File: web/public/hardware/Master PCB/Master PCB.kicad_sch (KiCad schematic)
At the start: 41 parts, among them J1 SWD Conn, J10 LED3, J11 LDR4, J12 LED4, J13 LED Conn, J2 OLED1, J3 OLED2, J4 5V_IN, J5 LDR1, J6 LED1, J7 LDR2, J8 LED2, J9 LDR3

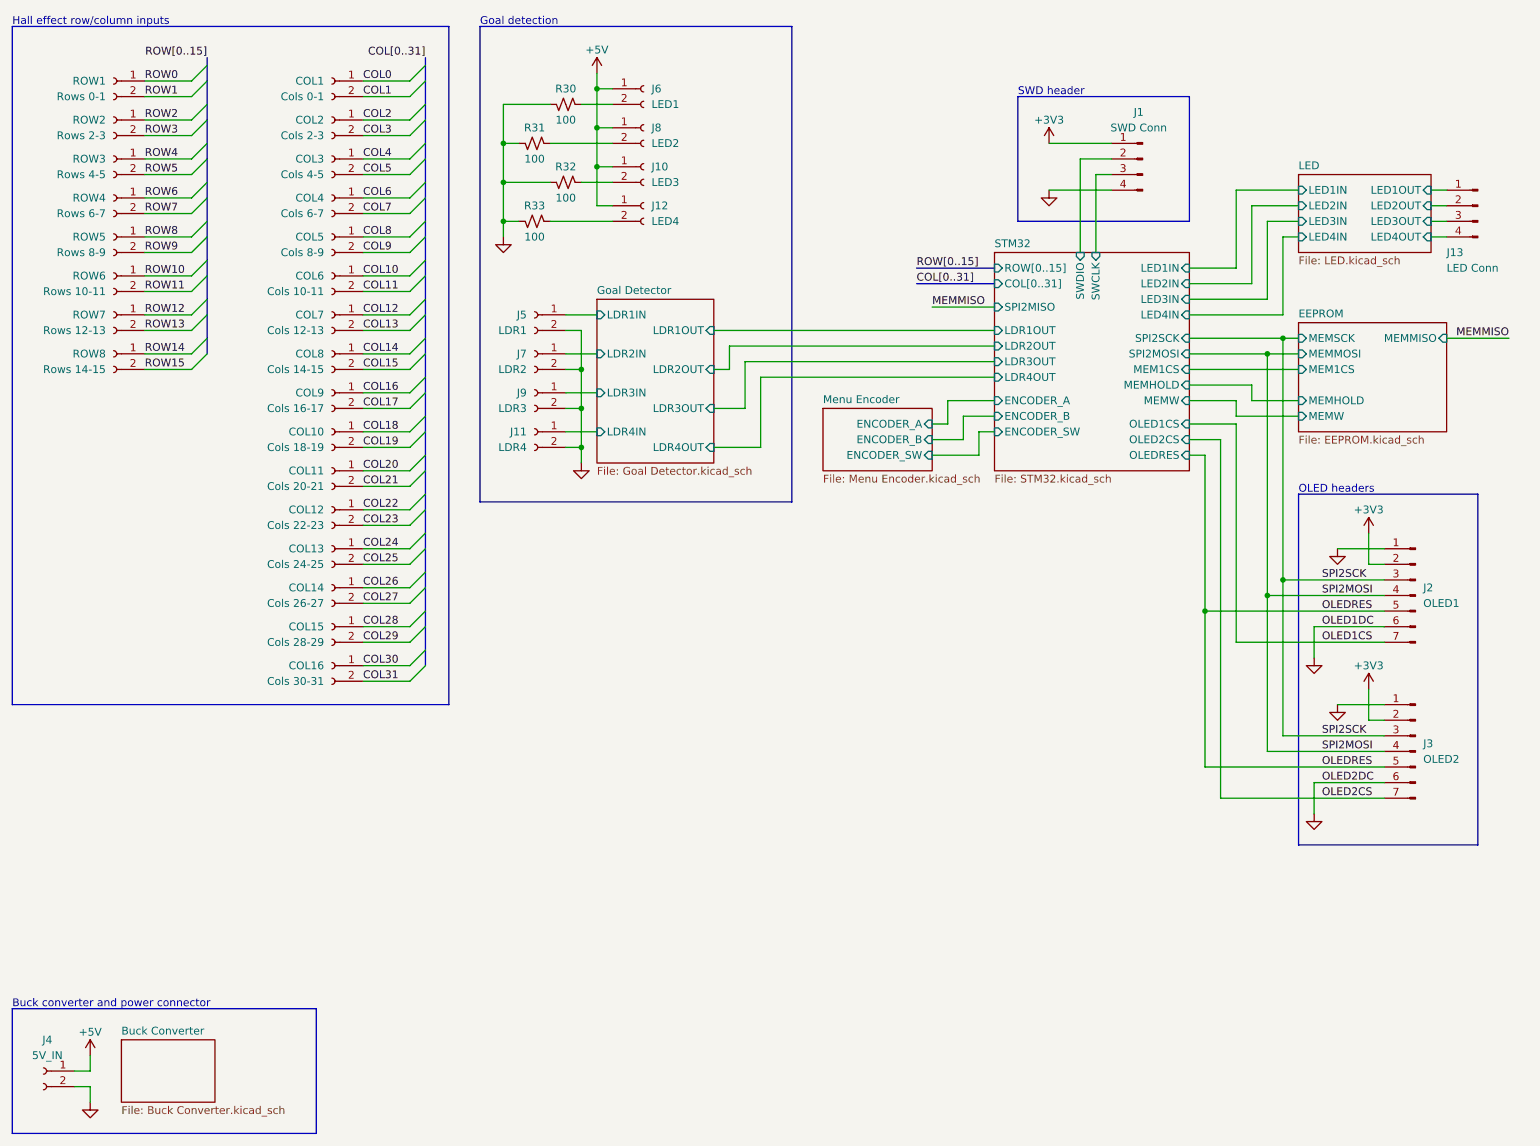
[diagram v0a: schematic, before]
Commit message: Add missing signals to master PCB for relay and OLED DC, add mounting holes, add text, add dimensions
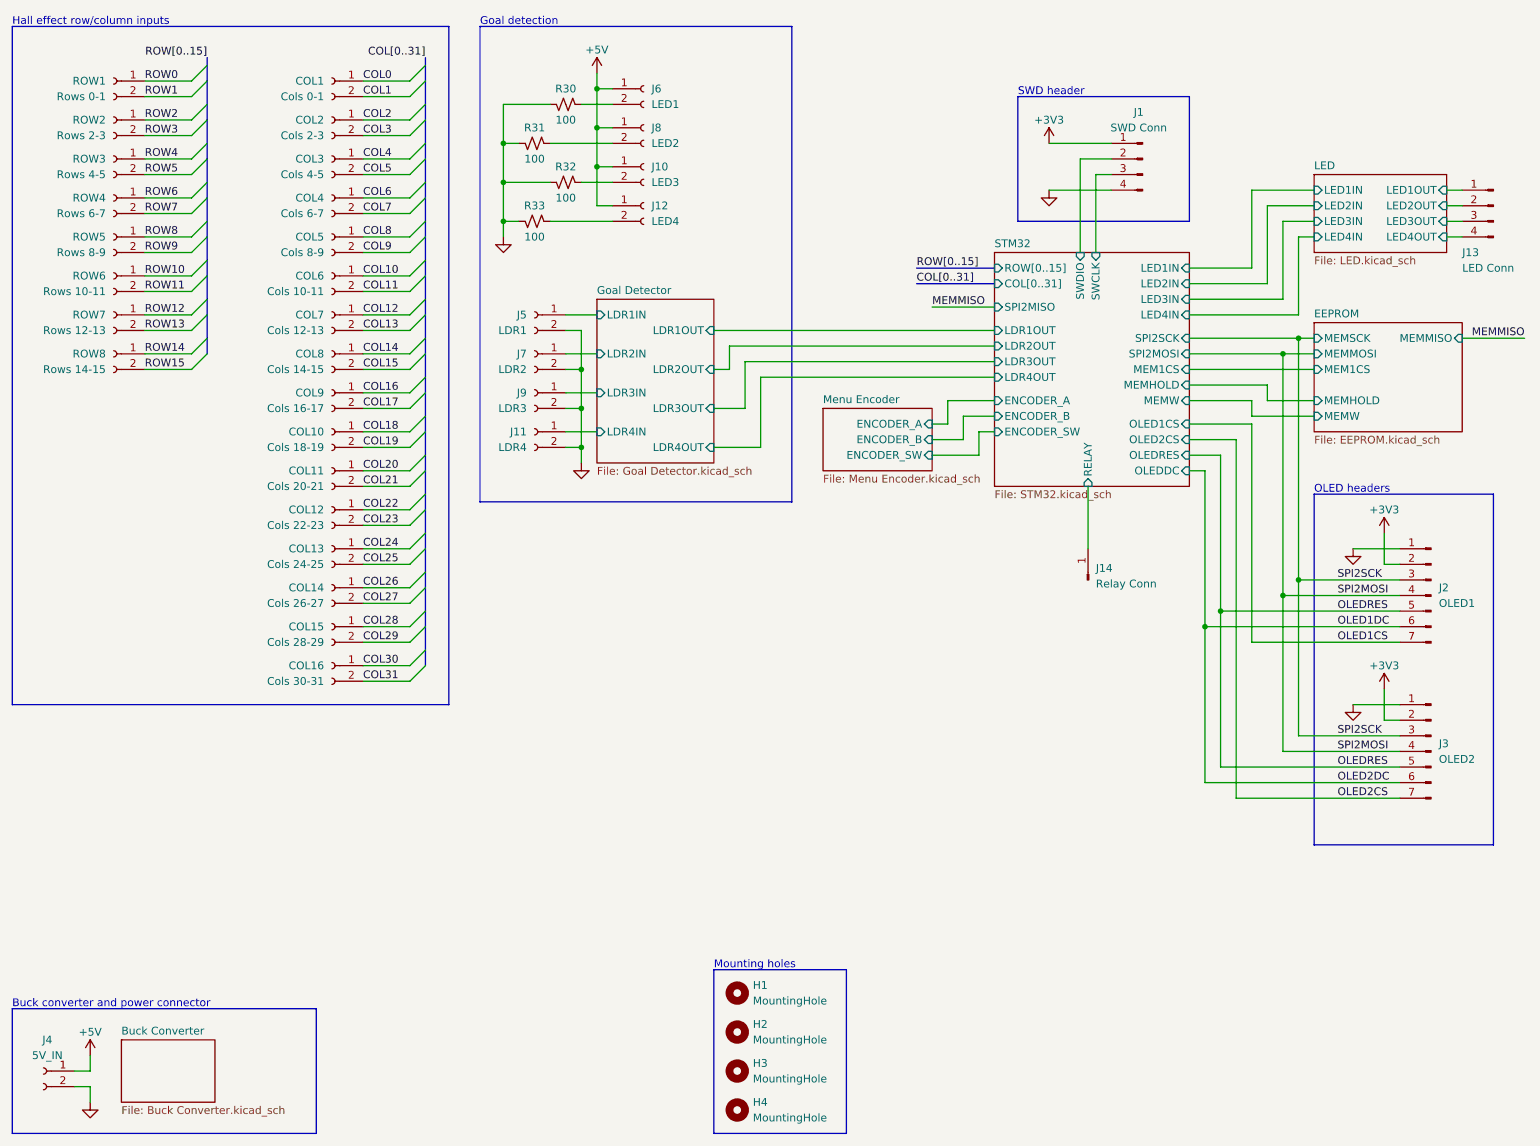
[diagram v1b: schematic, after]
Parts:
- added H1, H2, H3, H4: MountingHole, MountingHole:MountingHole_3.2mm_M3, symbol Mechanical:MountingHole
- added J14: Relay Conn, Connector_PinHeader_2.54mm:PinHeader_1x01_P2.54mm_Vertical, symbol Connector:Conn_01x01_Pin
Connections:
- net GND: no longer J2.6 (Pin_6), J3.6 (Pin_6)
- new net OLED1DC: J2.6 (Pin_6), J3.6 (Pin_6)
- new net STM32/RELAY: J14.1 (Pin_1)
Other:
- sheet STM32 ports: added OLEDDC, RELAY; removed none
- note added: "Mounting holes"
- moved on the sheet: J13, J2, J3

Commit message: Change STM32 pinout, begin placing components on new PCB
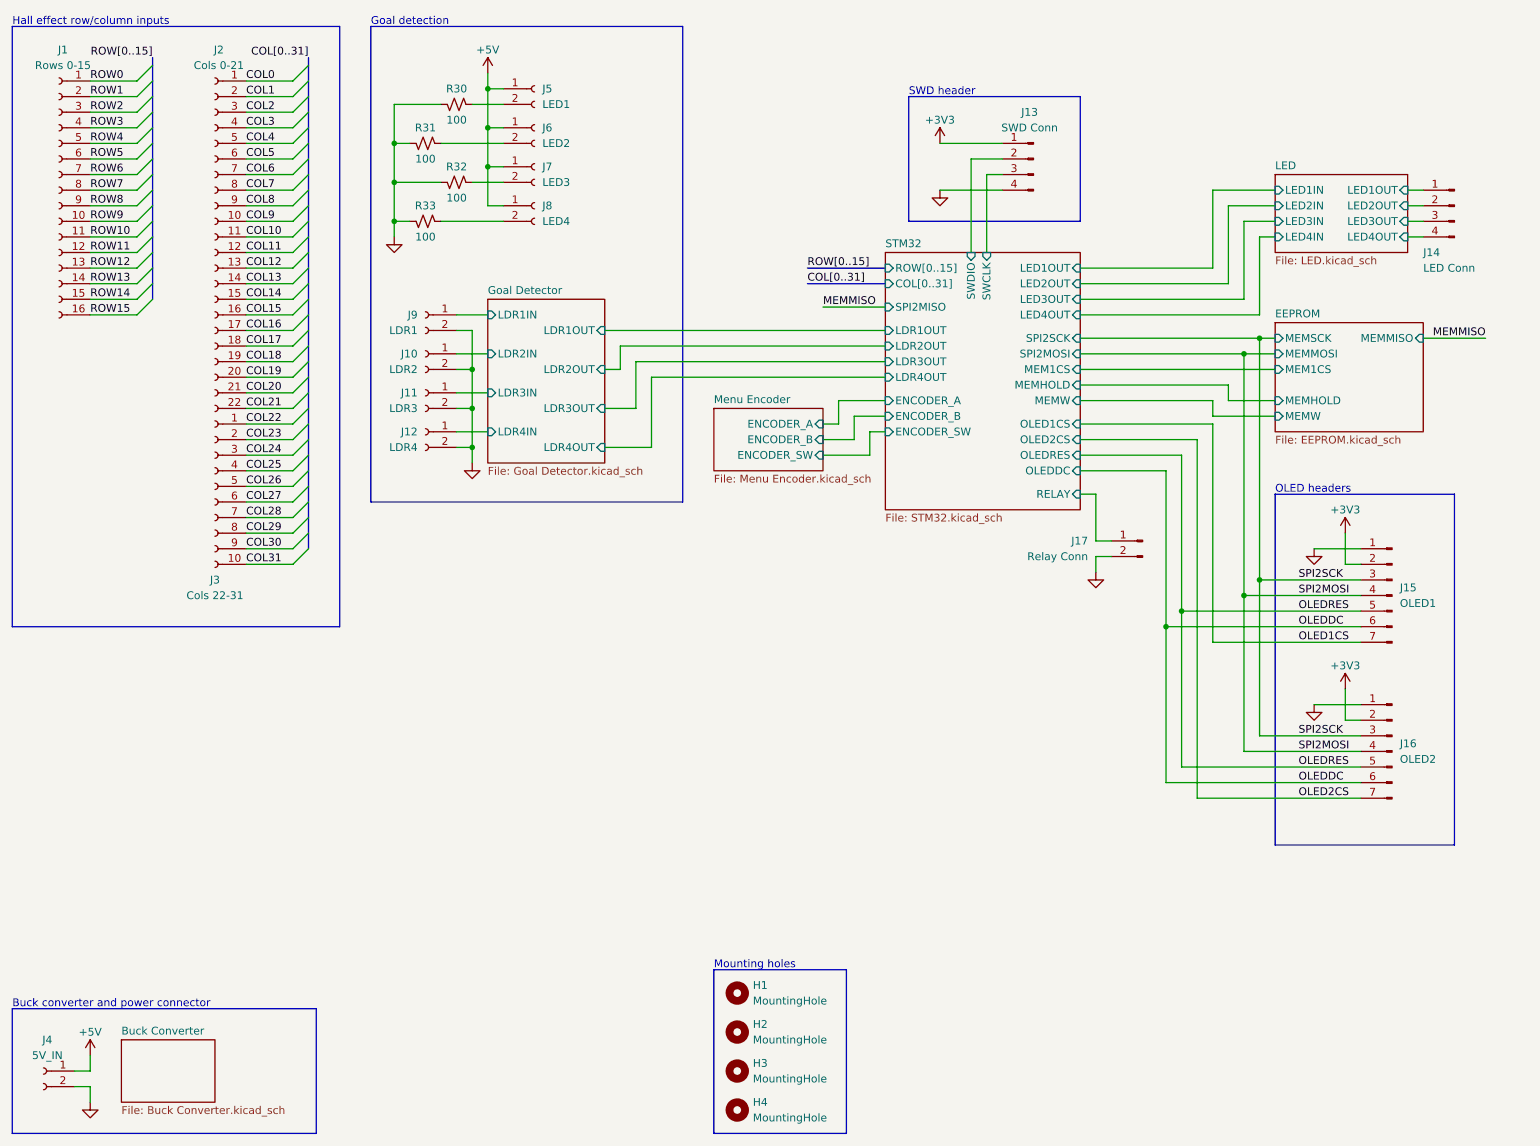
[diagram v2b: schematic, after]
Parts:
- removed COL1: Cols 0-1, Connector_PinHeader_2.54mm:PinHeader_1x02_P2.54mm_Vertical, symbol Connector:Conn_01x02_Socket
- removed COL10: Cols 18-19, Connector_PinHeader_2.54mm:PinHeader_1x02_P2.54mm_Vertical, symbol Connector:Conn_01x02_Socket
- removed COL11: Cols 20-21, Connector_PinHeader_2.54mm:PinHeader_1x02_P2.54mm_Vertical, symbol Connector:Conn_01x02_Socket
- removed COL12: Cols 22-23, Connector_PinHeader_2.54mm:PinHeader_1x02_P2.54mm_Vertical, symbol Connector:Conn_01x02_Socket
- removed COL13: Cols 24-25, Connector_PinHeader_2.54mm:PinHeader_1x02_P2.54mm_Vertical, symbol Connector:Conn_01x02_Socket
- removed COL14: Cols 26-27, Connector_PinHeader_2.54mm:PinHeader_1x02_P2.54mm_Vertical, symbol Connector:Conn_01x02_Socket
- removed COL15: Cols 28-29, Connector_PinHeader_2.54mm:PinHeader_1x02_P2.54mm_Vertical, symbol Connector:Conn_01x02_Socket
- removed COL16: Cols 30-31, Connector_PinHeader_2.54mm:PinHeader_1x02_P2.54mm_Vertical, symbol Connector:Conn_01x02_Socket
- removed COL2: Cols 2-3, Connector_PinHeader_2.54mm:PinHeader_1x02_P2.54mm_Vertical, symbol Connector:Conn_01x02_Socket
- removed COL3: Cols 4-5, Connector_PinHeader_2.54mm:PinHeader_1x02_P2.54mm_Vertical, symbol Connector:Conn_01x02_Socket
- removed COL4: Cols 6-7, Connector_PinHeader_2.54mm:PinHeader_1x02_P2.54mm_Vertical, symbol Connector:Conn_01x02_Socket
- removed COL5: Cols 8-9, Connector_PinHeader_2.54mm:PinHeader_1x02_P2.54mm_Vertical, symbol Connector:Conn_01x02_Socket
- removed COL6: Cols 10-11, Connector_PinHeader_2.54mm:PinHeader_1x02_P2.54mm_Vertical, symbol Connector:Conn_01x02_Socket
- removed COL7: Cols 12-13, Connector_PinHeader_2.54mm:PinHeader_1x02_P2.54mm_Vertical, symbol Connector:Conn_01x02_Socket
- removed COL8: Cols 14-15, Connector_PinHeader_2.54mm:PinHeader_1x02_P2.54mm_Vertical, symbol Connector:Conn_01x02_Socket
- removed COL9: Cols 16-17, Connector_PinHeader_2.54mm:PinHeader_1x02_P2.54mm_Vertical, symbol Connector:Conn_01x02_Socket
- removed J14: Relay Conn, Connector_PinHeader_2.54mm:PinHeader_1x01_P2.54mm_Vertical, symbol Connector:Conn_01x01_Pin
- removed ROW1: Rows 0-1, Connector_PinHeader_2.54mm:PinHeader_1x02_P2.54mm_Vertical, symbol Connector:Conn_01x02_Socket
- removed ROW2: Rows 2-3, Connector_PinHeader_2.54mm:PinHeader_1x02_P2.54mm_Vertical, symbol Connector:Conn_01x02_Socket
- removed ROW3: Rows 4-5, Connector_PinHeader_2.54mm:PinHeader_1x02_P2.54mm_Vertical, symbol Connector:Conn_01x02_Socket
- removed ROW4: Rows 6-7, Connector_PinHeader_2.54mm:PinHeader_1x02_P2.54mm_Vertical, symbol Connector:Conn_01x02_Socket
- removed ROW5: Rows 8-9, Connector_PinHeader_2.54mm:PinHeader_1x02_P2.54mm_Vertical, symbol Connector:Conn_01x02_Socket
- removed ROW6: Rows 10-11, Connector_PinHeader_2.54mm:PinHeader_1x02_P2.54mm_Vertical, symbol Connector:Conn_01x02_Socket
- removed ROW7: Rows 12-13, Connector_PinHeader_2.54mm:PinHeader_1x02_P2.54mm_Vertical, symbol Connector:Conn_01x02_Socket
- removed ROW8: Rows 14-15, Connector_PinHeader_2.54mm:PinHeader_1x02_P2.54mm_Vertical, symbol Connector:Conn_01x02_Socket
- added J1: Rows 0-15, Connector_PinHeader_2.54mm:PinHeader_1x16_P2.54mm_Vertical, symbol Connector:Conn_01x16_Socket
- added J17: Relay Conn, Connector_JST:JST_PH_S2B-PH-SM4-TB_1x02-1MP_P2.00mm_Horizontal, symbol Connector:Conn_01x02_Pin
- added J2: Cols 0-21, Connector_PinHeader_2.54mm:PinHeader_1x22_P2.54mm_Vertical, symbol Connector:Conn_01x22_Socket
- added J3: Cols 22-31, Connector_PinHeader_2.54mm:PinHeader_1x10_P2.54mm_Vertical, symbol Connector:Conn_01x10_Socket
- J10: renamed from J7; footprint Connector_PinHeader_2.54mm:PinHeader_1x02_P2.54mm_Vertical -> Connector_JST:JST_PH_S2B-PH-SM4-TB_1x02-1MP_P2.00mm_Horizontal
- J11: renamed from J9; footprint Connector_PinHeader_2.54mm:PinHeader_1x02_P2.54mm_Vertical -> Connector_JST:JST_PH_S2B-PH-SM4-TB_1x02-1MP_P2.00mm_Horizontal
- J12: renamed from J11; footprint Connector_PinHeader_2.54mm:PinHeader_1x02_P2.54mm_Vertical -> Connector_JST:JST_PH_S2B-PH-SM4-TB_1x02-1MP_P2.00mm_Horizontal
- J15: renamed from J2; footprint Connector_PinHeader_2.54mm:PinHeader_1x07_P2.54mm_Vertical -> Connector_JST:JST_PH_S7B-PH-SM4-TB_1x07-1MP_P2.00mm_Horizontal
- J16: renamed from J3; footprint Connector_PinHeader_2.54mm:PinHeader_1x07_P2.54mm_Vertical -> Connector_JST:JST_PH_S7B-PH-SM4-TB_1x07-1MP_P2.00mm_Horizontal
- J4: footprint Connector_PinHeader_2.54mm:PinHeader_1x02_P2.54mm_Vertical -> Connector_JST:JST_PH_S2B-PH-SM4-TB_1x02-1MP_P2.00mm_Horizontal
- J5: renamed from J6; footprint Connector_PinHeader_2.54mm:PinHeader_1x02_P2.54mm_Vertical -> Connector_JST:JST_PH_S2B-PH-SM4-TB_1x02-1MP_P2.00mm_Horizontal
- J6: renamed from J8; footprint Connector_PinHeader_2.54mm:PinHeader_1x02_P2.54mm_Vertical -> Connector_JST:JST_PH_S2B-PH-SM4-TB_1x02-1MP_P2.00mm_Horizontal
- J7: renamed from J10; footprint Connector_PinHeader_2.54mm:PinHeader_1x02_P2.54mm_Vertical -> Connector_JST:JST_PH_S2B-PH-SM4-TB_1x02-1MP_P2.00mm_Horizontal
- J8: renamed from J12; footprint Connector_PinHeader_2.54mm:PinHeader_1x02_P2.54mm_Vertical -> Connector_JST:JST_PH_S2B-PH-SM4-TB_1x02-1MP_P2.00mm_Horizontal
- J9: renamed from J5; footprint Connector_PinHeader_2.54mm:PinHeader_1x02_P2.54mm_Vertical -> Connector_JST:JST_PH_S2B-PH-SM4-TB_1x02-1MP_P2.00mm_Horizontal
- renumbered J1 to J13, J13 to J14
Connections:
- net COL0: now also J2.1 (Pin_1)
- net COL1: now also J2.2 (Pin_2)
- net COL10: now also J2.11 (Pin_11)
- net COL11: now also J2.12 (Pin_12)
- net COL12: now also J2.13 (Pin_13)
- net COL13: now also J2.14 (Pin_14)
- net COL14: now also J2.15 (Pin_15)
- net COL15: now also J2.16 (Pin_16)
- net COL16: now also J2.17 (Pin_17)
- net COL17: now also J2.18 (Pin_18)
- net COL18: now also J2.19 (Pin_19)
- net COL19: now also J2.20 (Pin_20)
- net COL2: now also J2.3 (Pin_3)
- net COL20: now also J2.21 (Pin_21)
- net COL21: now also J2.22 (Pin_22)
- net COL22: now also J3.1 (Pin_1)
- net COL23: now also J3.2 (Pin_2)
- net COL24: now also J3.3 (Pin_3)
- net COL25: now also J3.4 (Pin_4)
- net COL26: now also J3.5 (Pin_5)
- net COL27: now also J3.6 (Pin_6)
- net COL28: now also J3.7 (Pin_7)
- net COL29: now also J3.8 (Pin_8)
- net COL3: now also J2.4 (Pin_4)
- net COL30: now also J3.9 (Pin_9)
- net COL31: now also J3.10 (Pin_10)
- net COL4: now also J2.5 (Pin_5)
- net COL5: now also J2.6 (Pin_6)
- net COL6: now also J2.7 (Pin_7)
- net COL7: now also J2.8 (Pin_8)
- net COL8: now also J2.9 (Pin_9)
- net COL9: now also J2.10 (Pin_10)
- net GND: now also J17.2 (Pin_2)
- net ROW0: now also J1.1 (Pin_1)
- net ROW1: now also J1.2 (Pin_2)
- net ROW10: now also J1.11 (Pin_11)
- net ROW11: now also J1.12 (Pin_12)
- net ROW12: now also J1.13 (Pin_13)
- net ROW13: now also J1.14 (Pin_14)
- net ROW14: now also J1.15 (Pin_15)
- net ROW15: now also J1.16 (Pin_16)
- net ROW2: now also J1.3 (Pin_3)
- net ROW3: now also J1.4 (Pin_4)
- net ROW4: now also J1.5 (Pin_5)
- net ROW5: now also J1.6 (Pin_6)
- net ROW6: now also J1.7 (Pin_7)
- net ROW7: now also J1.8 (Pin_8)
- net ROW8: now also J1.9 (Pin_9)
- net ROW9: now also J1.10 (Pin_10)
- net STM32/RELAY: now also J17.1 (Pin_1)
- net OLED1DC renamed OLEDDC
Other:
- sheet STM32 ports: added LED1OUT, LED2OUT, LED3OUT, LED4OUT; removed LED1IN, LED2IN, LED3IN, LED4IN
- moved on the sheet: J10, J11, J12, J13, J14, J15, J16, J5, J6, J7, J8, J9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

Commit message: Switch JST to THT
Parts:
- J10, J11, J12, J17, J4, J5, J6, J7, J8, J9: footprint Connector_JST:JST_PH_S2B-PH-SM4-TB_1x02-1MP_P2.00mm_Horizontal -> Connector_JST:JST_PH_B2B-PH-K_1x02_P2.00mm_Vertical
- J15, J16: footprint Connector_JST:JST_PH_S7B-PH-SM4-TB_1x07-1MP_P2.00mm_Horizontal -> Connector_JST:JST_PH_B7B-PH-K_1x07_P2.00mm_Vertical
